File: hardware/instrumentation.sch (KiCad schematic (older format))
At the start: 5 parts

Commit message: Added TMUX1309 symbol
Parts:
- added U?: TMUX1309, Package_DFN_QFN:WQFN-16-1EP_3x3mm_P0.5mm_EP1.6x1.6mm, symbol mallard:TMUX1309
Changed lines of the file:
@@
+	1    0    0    -1
+$EndComp
+$Comp
+L mallard:TMUX1309 U?
+U 1 1 610A2355
+P 6250 750
+F 0 "U?" H 6250 875 50  0000 C CNN
+F 1 "TMUX1309" H 6250 784 50  0000 C CNN
+F 2 "Package_DFN_QFN:WQFN-16-1EP_3x3mm_P0.5mm_EP1.6x1.6mm" H 6250 -1150 50  0001 C CNN
+F 3 "https://www.ti.com/lit/ds/symlink/tmux1309.pdf" H 6250 750 50  0001 C CNN
+	1    6250 750
 	1    0    0    -1
 $EndComp

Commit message: Added Instrumentation Circuits
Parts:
- removed U?: SN74HCS153, symbol mallard:SN74HCS153
- added 10k (x4), 1k, 20k (x2), 30k, 9k: R, symbol Device:R
- added Eh1, Eh2, Eh3: Eh Electrode, symbol Connector_Generic:Conn_01x01
- added MUX2: TMUX1309, Package_DFN_QFN:WQFN-16-1EP_3x3mm_P0.5mm_EP1.6x1.6mm, symbol mallard:TMUX1309
- added Ref1: Ref Electrode, symbol Connector_Generic:Conn_01x01
- added SM1, SM2, SM3: Oct Soil Moisture, symbol Connector_Generic:Conn_01x03
- gave numbers to parts that had none: 5
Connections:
- net labels added: +1V0, +3V3, -3V3, GND, VDD
- wire segments 0 -> 68
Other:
- note added: "Eh Sensor Output"
- note added: "Reference Electrode Output"
- note added: "Soil Moisture Output"
- note added: "Temperature Sensor Output"
- moved on the sheet: MUX1, OP1, Temp1, Temp2, Temp3

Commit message: Added all Digikey part numbers. Started MC schematic. Fixed the reference number on some symbols.
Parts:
- removed 10k (x4), 1k, 20k (x2), 30k, 9k: R, symbol Device:R
- removed MUX1, MUX2: TMUX1309, Package_DFN_QFN:WQFN-16-1EP_3x3mm_P0.5mm_EP1.6x1.6mm, symbol mallard:TMUX1309
- removed OP1: LMV554, symbol mallard:LMV554
- removed Temp1, Temp2, Temp3: TMP235, symbol mallard:TMP235
- added R10: 9.1k, symbol Device:R
- added R11, R8: 20k, symbol Device:R
- added R3, R4, R5, R9: 10k, symbol Device:R
- added R6: 1k, symbol Device:R
- added R7: 30k, symbol Device:R
- added U2, U3: TMUX1309, Package_DFN_QFN:WQFN-16-1EP_3x3mm_P0.5mm_EP1.6x1.6mm, symbol mallard:TMUX1309
- added U4: LMV554, symbol mallard:LMV554
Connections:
- net labels added: Eh_Sense, Moisture_Sense, Ref_Out, Temp_Sense
- net labels removed: VDD
- wire segments 68 -> 61
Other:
- note added: "Needed New Temp sensors\n"
- note removed: "Eh Sensor Output"
- note removed: "Reference Electrode Output"
- note removed: "Temperature Sensor Output"

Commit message: Finished MC design
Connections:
- net MUX1_A1: now reaches U2.10 (A0)
- net MUX1_EN: now reaches U2.6 (EN)
- net MUX1_A0: now reaches U2.9 (A1)
- net MUX2_A1: now reaches U3.10 (A0)
- net MUX2_EN: now reaches U3.6 (EN)
- net MUX2_A0: now reaches U3.9 (A1)
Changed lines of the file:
@@
 	2800 2550 4150 2550
 Wire Wire Line
-	3550 1900 3550 2450
-Wire Wire Line
-	3800 1250 3800 2350
+	3100 1900 3100 2450
+Wire Wire Line
+	3300 1250 3300 2350
 Wire Wire Line
 	2800 3350 3250 3350
@@
 	3750 3050 4150 3050
 Wire Wire Line
-	3800 2350 4150 2350
-Wire Wire Line
-	2800 1250 3800 1250
-Wire Wire Line
-	3550 2450 4150 2450
-Wire Wire Line
-	2800 1900 3550 1900
+	3300 2350 4150 2350
+Wire Wire Line
+	2800 1250 3300 1250
+Wire Wire Line
+	3100 2450 4150 2450
+Wire Wire Line
+	2800 1900 3100 1900
 Wire Wire Line
 	5100 2850 4950 2850
@@
 Text Notes 2850 4800 0    50   ~ 0
 Needed New Temp sensors\n
+Text GLabel 4050 1850 0    50   Input ~ 0
+MUX1_EN
+Text GLabel 4050 2050 0    50   Input ~ 0
+MUX1_A0
+Text GLabel 4050 2150 0    50   Input ~ 0
+MUX1_A1
+Wire Wire Line
+	4150 1850 4050 1850
+Wire Wire Line
+	4150 2050 4050 2050
+Wire Wire Line
+	4150 2150 4050 2150
+Text GLabel 4100 4250 0    50   Input ~ 0
+MUX2_EN
+Wire Wire Line
+	4100 4250 4200 4250
+Text GLabel 4100 4450 0    50   Input ~ 0
+MUX2_A0
+Text GLabel 4100 4550 0    50   Input ~ 0
+MUX2_A1
+Wire Wire Line
+	4200 4450 4100 4450
+Wire Wire Line
+	4200 4550 4100 4550
 $EndSCHEMATC

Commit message: Not sure what changes I made sry
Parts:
- U4: Digikey LMP7721MA/NOPB-ND‎ -> (none)
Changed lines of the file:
@@
 F 2 "" H 7500 1600 50  0001 C CNN
 F 3 "https://www.ti.com/lit/ds/symlink/lmv551.pdf?HQS=dis-dk-null-digikeymode-dsf-pf-null-wwe&ts=1626469395066&ref_url=https%253A%252F%252Fwww.ti.com%252Fgeneral%252Fdocs%252Fsuppproductinfo.tsp%253FdistId%253D10%2526gotoUrl%253Dhttps%253A%252F%252Fwww.ti.com%252Flit%252Fgpn%252Flmv551" H 7500 1600 50  0001 C CNN
-F 4 "LMP7721MA/NOPB-ND‎" H 7500 2500 50  0001 C CNN "Digikey"
+F 4 "" H 7500 2500 50  0001 C CNN "Digikey"
 	1    7500 2500
 	1    0    0    -1

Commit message: House Keeping Tasks
 - Modified parts list parameters for various parts
 - Assigned Ref Des to components
 - Changed TPS717 symbol and feedback resistors
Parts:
- R10, R11, R4, R6, R7, R8: footprint (none) -> Resistor_SMD:R_0201_0603Metric_Pad0.64x0.40mm_HandSolder
- R3, R5, R9: footprint (none) -> Resistor_SMD:R_0201_0603Metric_Pad0.64x0.40mm_HandSolder; Manufacturer ‎RC0603DR-0710KL‎ -> (none)
- U4: footprint (none) -> Package_SO:TSSOP-14_4.4x5mm_P0.65mm; Digikey (none) -> 296-51370-1-ND
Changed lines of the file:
@@
 F 0 "R3" V 5043 2850 50  0000 C CNN
 F 1 "10k" V 5134 2850 50  0000 C CNN
-F 2 "" V 5180 2850 50  0001 C CNN
-F 3 "~" H 5250 2850 50  0001 C CNN
+F 2 "Resistor_SMD:R_0201_0603Metric_Pad0.64x0.40mm_HandSolder" V 5180 2850 50  0001 C CNN
+F 3 "https://www.yageo.com/upload/media/product/productsearch/datasheet/rchip/PYu-RC_Group_51_RoHS_L_11.pdf" H 5250 2850 50  0001 C CNN
 F 4 "13-RC0603DR-0710KLCT-ND‎" V 5250 2850 50  0001 C CNN "Digikey"
-F 5 "‎RC0603DR-0710KL‎" V 5250 2850 50  0001 C CNN "Manufacturer"
 	1    5250 2850
 	0    1    1    0
@@
 F 0 "R8" V 7243 1750 50  0000 C CNN
 F 1 "20k" V 7334 1750 50  0000 C CNN
-F 2 "" V 7380 1750 50  0001 C CNN
-F 3 "~" H 7450 1750 50  0001 C CNN
+F 2 "Resistor_SMD:R_0201_0603Metric_Pad0.64x0.40mm_HandSolder" V 7380 1750 50  0001 C CNN
+F 3 "https://industrial.panasonic.com/cdbs/www-data/pdf/RDM0000/AOA0000C328.pdf" H 7450 1750 50  0001 C CNN
 F 4 "‎P20429CT-ND‎" V 7450 1750 50  0001 C CNN "Digikey"
 	1    7450 1750
@@
 F 0 "R7" V 7243 1350 50  0000 C CNN
 F 1 "30k" V 7334 1350 50  0000 C CNN
-F 2 "" V 7380 1350 50  0001 C CNN
-F 3 "~" H 7450 1350 50  0001 C CNN
+F 2 "Resistor_SMD:R_0201_0603Metric_Pad0.64x0.40mm_HandSolder" V 7380 1350 50  0001 C CNN
+F 3 "https://www.yageo.com/upload/media/product/productsearch/datasheet/rchip/PYu-RT_1-to-0.01_RoHS_L_12.pdf" H 7450 1350 50  0001 C CNN
 F 4 "311-30KDCT-ND‎" V 7450 1350 50  0001 C CNN "Digikey"
 	1    7450 1350
@@
 F 0 "U4" H 7500 2675 50  0000 C CNN
 F 1 "LMV554" H 7500 2584 50  0000 C CNN
-F 2 "" H 7500 1600 50  0001 C CNN
+F 2 "Package_SO:TSSOP-14_4.4x5mm_P0.65mm" H 7500 1600 50  0001 C CNN
 F 3 "https://www.ti.com/lit/ds/symlink/lmv551.pdf?HQS=dis-dk-null-digikeymode-dsf-pf-null-wwe&ts=1626469395066&ref_url=https%253A%252F%252Fwww.ti.com%252Fgeneral%252Fdocs%252Fsuppproductinfo.tsp%253FdistId%253D10%2526gotoUrl%253Dhttps%253A%252F%252Fwww.ti.com%252Flit%252Fgpn%252Flmv551" H 7500 1600 50  0001 C CNN
-F 4 "" H 7500 2500 50  0001 C CNN "Digikey"
+F 4 "296-51370-1-ND" H 7500 2500 50  0001 C CNN "Digikey"
 	1    7500 2500
 	1    0    0    -1
@@
 F 0 "R6" H 7120 5146 50  0000 L CNN
 F 1 "1k" H 7120 5055 50  0000 L CNN
-F 2 "" V 6980 5100 50  0001 C CNN
-F 3 "~" H 7050 5100 50  0001 C CNN
+F 2 "Resistor_SMD:R_0201_0603Metric_Pad0.64x0.40mm_HandSolder" V 6980 5100 50  0001 C CNN
+F 3 "https://www.vishay.com/docs/20065/rcse3.pdf" H 7050 5100 50  0001 C CNN
 F 4 "541-2788-1-ND" H 7050 5100 50  0001 C CNN "Digikey"
 	1    7050 5100
@@
 F 0 "R10" V 7293 4850 50  0000 C CNN
 F 1 "9.1k" V 7384 4850 50  0000 C CNN
-F 2 "" V 7430 4850 50  0001 C CNN
-F 3 "~" H 7500 4850 50  0001 C CNN
+F 2 "Resistor_SMD:R_0201_0603Metric_Pad0.64x0.40mm_HandSolder" V 7430 4850 50  0001 C CNN
+F 3 "https://www.yageo.com/upload/media/product/productsearch/datasheet/rchip/PYu-RT_1-to-0.01_RoHS_L_12.pdf" H 7500 4850 50  0001 C CNN
 F 4 "YAG1756CT-ND‎" H 7500 4850 50  0001 C CNN "Digikey"
 	1    7500 4850
@@
 F 0 "R4" H 5830 2554 50  0000 R CNN
 F 1 "10k" H 5830 2645 50  0000 R CNN
-F 2 "" V 5830 2600 50  0001 C CNN
-F 3 "~" H 5900 2600 50  0001 C CNN
+F 2 "Resistor_SMD:R_0201_0603Metric_Pad0.64x0.40mm_HandSolder" V 5830 2600 50  0001 C CNN
+F 3 "https://www.yageo.com/upload/media/product/productsearch/datasheet/rchip/PYu-RC_Group_51_RoHS_L_11.pdf" H 5900 2600 50  0001 C CNN
 F 4 "13-RC0603DR-0710KLCT-ND‎" V 5900 2600 50  0001 C CNN "Digikey"
 	1    5900 2600
@@
 F 0 "R9" V 7243 2150 50  0000 C CNN
 F 1 "10k" V 7334 2150 50  0000 C CNN
-F 2 "" V 7380 2150 50  0001 C CNN
-F 3 "~" H 7450 2150 50  0001 C CNN
+F 2 "Resistor_SMD:R_0201_0603Metric_Pad0.64x0.40mm_HandSolder" V 7380 2150 50  0001 C CNN
+F 3 "https://www.yageo.com/upload/media/product/productsearch/datasheet/rchip/PYu-RC_Group_51_RoHS_L_11.pdf" H 7450 2150 50  0001 C CNN
 F 4 "13-RC0603DR-0710KLCT-ND‎" V 7450 2150 50  0001 C CNN "Digikey"
-F 5 "‎RC0603DR-0710KL‎" V 7450 2150 50  0001 C CNN "Manufacturer"
 	1    7450 2150
 	0    1    1    0
@@
 F 0 "R5" H 6730 5854 50  0000 R CNN
 F 1 "10k" H 6730 5945 50  0000 R CNN
-F 2 "" V 6730 5900 50  0001 C CNN
-F 3 "~" H 6800 5900 50  0001 C CNN
+F 2 "Resistor_SMD:R_0201_0603Metric_Pad0.64x0.40mm_HandSolder" V 6730 5900 50  0001 C CNN
+F 3 "https://www.yageo.com/upload/media/product/productsearch/datasheet/rchip/PYu-RC_Group_51_RoHS_L_11.pdf" H 6800 5900 50  0001 C CNN
 F 4 "13-RC0603DR-0710KLCT-ND‎" V 6800 5900 50  0001 C CNN "Digikey"
-F 5 "‎RC0603DR-0710KL‎" V 6800 5900 50  0001 C CNN "Manufacturer"
 	1    6800 5900
 	-1   0    0    1
@@
 F 0 "R11" V 7293 5600 50  0000 C CNN
 F 1 "20k" V 7384 5600 50  0000 C CNN
-F 2 "" V 7430 5600 50  0001 C CNN
-F 3 "~" H 7500 5600 50  0001 C CNN
+F 2 "Resistor_SMD:R_0201_0603Metric_Pad0.64x0.40mm_HandSolder" V 7430 5600 50  0001 C CNN
+F 3 "https://industrial.panasonic.com/cdbs/www-data/pdf/RDM0000/AOA0000C328.pdf" H 7500 5600 50  0001 C CNN
 F 4 "‎P20429CT-ND‎" V 7500 5600 50  0001 C CNN "Digikey"
 	1    7500 5600

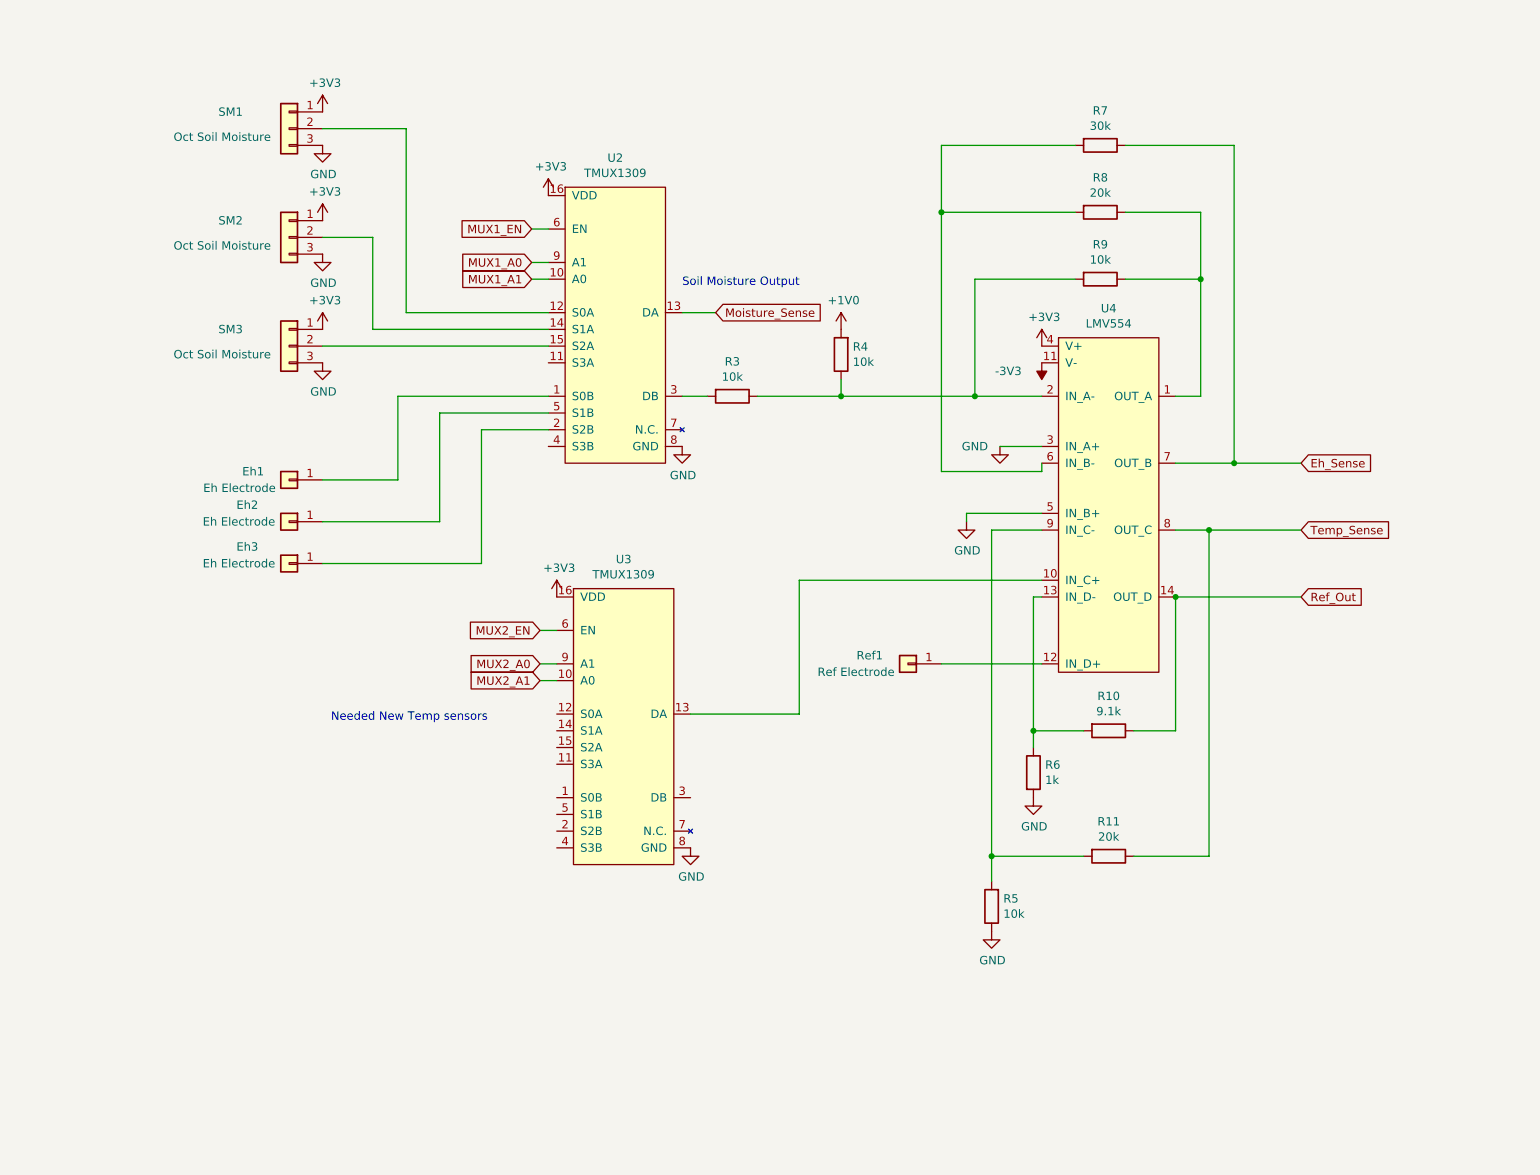
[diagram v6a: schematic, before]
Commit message: Added more ref des
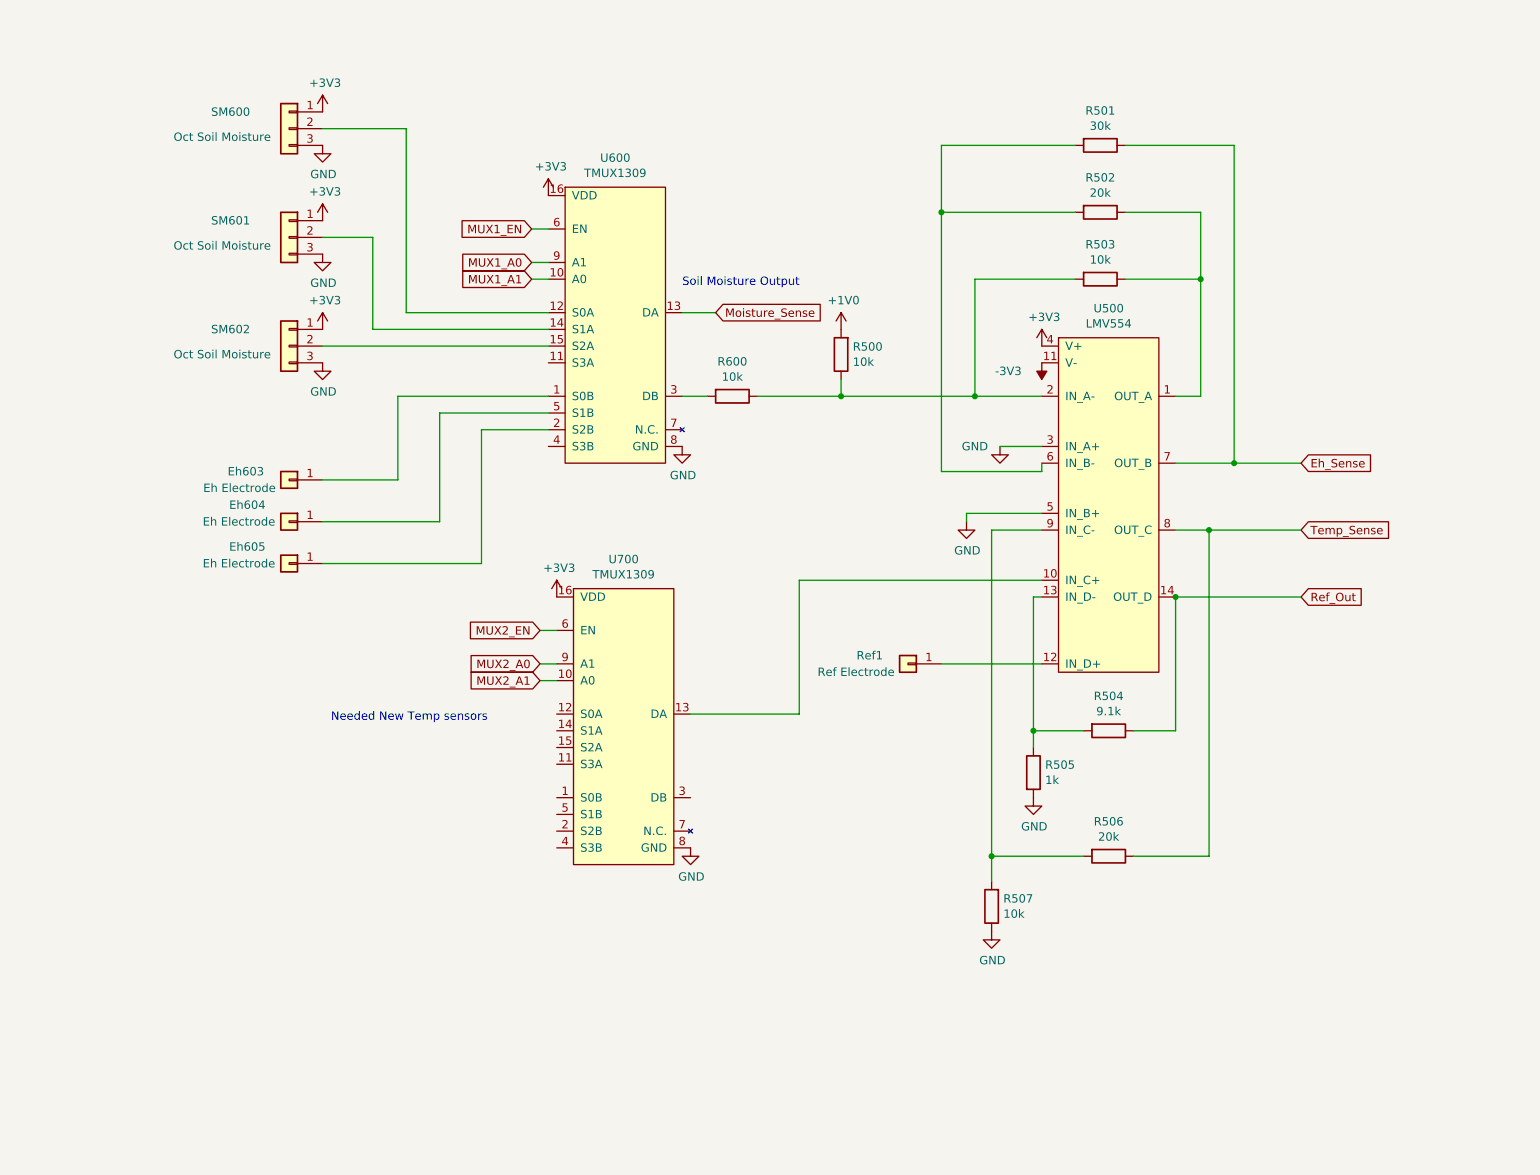
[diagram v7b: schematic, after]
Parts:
- renumbered Eh1 to Eh603, Eh2 to Eh604, Eh3 to Eh605, R4 to R500, R7 to R501, R8 to R502, R9 to R503, R10 to R504, R6 to R505, R11 to R506, R5 to R507, R3 to R600, SM1 to SM600, SM2 to SM601, SM3 to SM602, U4 to U500, U2 to U600, U3 to U700
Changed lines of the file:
@@
 $EndComp
 $Comp
-L Connector_Generic:Conn_01x01 Eh1
+L Connector_Generic:Conn_01x01 Eh603
 U 1 1 610DC20D
 P 2600 3350
-F 0 "Eh1" H 2750 3400 50  0000 L CNN
+F 0 "Eh603" H 2750 3400 50  0000 L CNN
 F 1 "Eh Electrode" H 2680 3301 50  0000 L CNN
 F 2 "" H 2600 3350 50  0001 C CNN
@@
 $EndComp
 $Comp
-L Connector_Generic:Conn_01x01 Eh2
+L Connector_Generic:Conn_01x01 Eh604
 U 1 1 610DD4BF
 P 2600 3600
-F 0 "Eh2" H 2850 3700 50  0000 C CNN
+F 0 "Eh604" H 2850 3700 50  0000 C CNN
 F 1 "Eh Electrode" H 2900 3600 50  0000 C CNN
 F 2 "" H 2600 3600 50  0001 C CNN
@@
 $EndComp
 $Comp
-L Connector_Generic:Conn_01x01 Eh3
+L Connector_Generic:Conn_01x01 Eh605
 U 1 1 610DDA62
 P 2600 3850
-F 0 "Eh3" H 2850 3950 50  0000 C CNN
+F 0 "Eh605" H 2850 3950 50  0000 C CNN
 F 1 "Eh Electrode" H 2900 3850 50  0000 C CNN
 F 2 "" H 2600 3850 50  0001 C CNN
@@
 $EndComp
 $Comp
-L Connector_Generic:Conn_01x03 SM1
+L Connector_Generic:Conn_01x03 SM600
 U 1 1 610E87B7
 P 2600 1250
-F 0 "SM1" H 2950 1350 50  0000 C CNN
+F 0 "SM600" H 2950 1350 50  0000 C CNN
 F 1 "Oct Soil Moisture " H 3000 1200 50  0000 C CNN
 F 2 "" H 2600 1250 50  0001 C CNN
@@
 $EndComp
 $Comp
-L Connector_Generic:Conn_01x03 SM2
+L Connector_Generic:Conn_01x03 SM601
 U 1 1 610F5909
 P 2600 1900
-F 0 "SM2" H 2950 2000 50  0000 C CNN
+F 0 "SM601" H 2950 2000 50  0000 C CNN
 F 1 "Oct Soil Moisture " H 3000 1850 50  0000 C CNN
 F 2 "" H 2600 1900 50  0001 C CNN
@@
 $EndComp
 $Comp
-L Connector_Generic:Conn_01x03 SM3
+L Connector_Generic:Conn_01x03 SM602
 U 1 1 610F6592
 P 2600 2550
-F 0 "SM3" H 2950 2650 50  0000 C CNN
+F 0 "SM602" H 2950 2650 50  0000 C CNN
 F 1 "Oct Soil Moisture " H 3000 2500 50  0000 C CNN
 F 2 "" H 2600 2550 50  0001 C CNN
@@
 	6850 3150 7100 3150
 $Comp
-L mallard:TMUX1309 U2
+L mallard:TMUX1309 U600
 U 1 1 61595D93
 P 4550 1550
-F 0 "U2" H 4550 1675 50  0000 C CNN
+F 0 "U600" H 4550 1675 50  0000 C CNN
 F 1 "TMUX1309" H 4550 1584 50  0000 C CNN
 F 2 "Package_DFN_QFN:WQFN-16-1EP_3x3mm_P0.5mm_EP1.6x1.6mm" H 4550 -350 50  0001 C CNN
@@
 $EndComp
 $Comp
-L Device:R R3
+L Device:R R600
 U 1 1 6159B70F
 P 5250 2850
-F 0 "R3" V 5043 2850 50  0000 C CNN
+F 0 "R600" V 5043 2850 50  0000 C CNN
 F 1 "10k" V 5134 2850 50  0000 C CNN
 F 2 "Resistor_SMD:R_0201_0603Metric_Pad0.64x0.40mm_HandSolder" V 5180 2850 50  0001 C CNN
@@
 $EndComp
 $Comp
-L Device:R R8
+L Device:R R502
 U 1 1 6159EF44
 P 7450 1750
-F 0 "R8" V 7243 1750 50  0000 C CNN
+F 0 "R502" V 7243 1750 50  0000 C CNN
 F 1 "20k" V 7334 1750 50  0000 C CNN
 F 2 "Resistor_SMD:R_0201_0603Metric_Pad0.64x0.40mm_HandSolder" V 7380 1750 50  0001 C CNN
@@
 $EndComp
 $Comp
-L Device:R R7
+L Device:R R501
 U 1 1 615A0EFD
 P 7450 1350
-F 0 "R7" V 7243 1350 50  0000 C CNN
+F 0 "R501" V 7243 1350 50  0000 C CNN
 F 1 "30k" V 7334 1350 50  0000 C CNN
 F 2 "Resistor_SMD:R_0201_0603Metric_Pad0.64x0.40mm_HandSolder" V 7380 1350 50  0001 C CNN
@@
 $EndComp
 $Comp
-L mallard:LMV554 U4
+L mallard:LMV554 U500
 U 1 1 615A28E5
 P 7500 2500
-F 0 "U4" H 7500 2675 50  0000 C CNN
+F 0 "U500" H 7500 2675 50  0000 C CNN
 F 1 "LMV554" H 7500 2584 50  0000 C CNN
 F 2 "Package_SO:TSSOP-14_4.4x5mm_P0.65mm" H 7500 1600 50  0001 C CNN
@@
 Connection ~ 7900 4050
 $Comp
-L Device:R R6
+L Device:R R505
 U 1 1 615A675D
 P 7050 5100
-F 0 "R6" H 7120 5146 50  0000 L CNN
+F 0 "R505" H 7120 5146 50  0000 L CNN
 F 1 "1k" H 7120 5055 50  0000 L CNN
 F 2 "Resistor_SMD:R_0201_0603Metric_Pad0.64x0.40mm_HandSolder" V 6980 5100 50  0001 C CNN
@@
 $EndComp
 $Comp
-L Device:R R10
+L Device:R R504
 U 1 1 615A70C7
 P 7500 4850
-F 0 "R10" V 7293 4850 50  0000 C CNN
+F 0 "R504" V 7293 4850 50  0000 C CNN
 F 1 "9.1k" V 7384 4850 50  0000 C CNN
 F 2 "Resistor_SMD:R_0201_0603Metric_Pad0.64x0.40mm_HandSolder" V 7430 4850 50  0001 C CNN
@@
 $EndComp
 $Comp
-L Device:R R4
+L Device:R R500
 U 1 1 615A7B6B
 P 5900 2600
-F 0 "R4" H 5830 2554 50  0000 R CNN
+F 0 "R500" H 5830 2554 50  0000 R CNN
 F 1 "10k" H 5830 2645 50  0000 R CNN
 F 2 "Resistor_SMD:R_0201_0603Metric_Pad0.64x0.40mm_HandSolder" V 5830 2600 50  0001 C CNN
@@
 $EndComp
 $Comp
-L Device:R R9
+L Device:R R503
 U 1 1 615A829C
 P 7450 2150
-F 0 "R9" V 7243 2150 50  0000 C CNN
+F 0 "R503" V 7243 2150 50  0000 C CNN
 F 1 "10k" V 7334 2150 50  0000 C CNN
 F 2 "Resistor_SMD:R_0201_0603Metric_Pad0.64x0.40mm_HandSolder" V 7380 2150 50  0001 C CNN
@@
 $EndComp
 $Comp
-L Device:R R5
+L Device:R R507
 U 1 1 615A8D1F
 P 6800 5900
-F 0 "R5" H 6730 5854 50  0000 R CNN
+F 0 "R507" H 6730 5854 50  0000 R CNN
 F 1 "10k" H 6730 5945 50  0000 R CNN
 F 2 "Resistor_SMD:R_0201_0603Metric_Pad0.64x0.40mm_HandSolder" V 6730 5900 50  0001 C CNN
@@
 $EndComp
 $Comp
-L Device:R R11
+L Device:R R506
 U 1 1 615AA078
 P 7500 5600
-F 0 "R11" V 7293 5600 50  0000 C CNN
+F 0 "R506" V 7293 5600 50  0000 C CNN
 F 1 "20k" V 7384 5600 50  0000 C CNN
 F 2 "Resistor_SMD:R_0201_0603Metric_Pad0.64x0.40mm_HandSolder" V 7430 5600 50  0001 C CNN
@@
 Ref_Out
 $Comp
-L mallard:TMUX1309 U3
+L mallard:TMUX1309 U700
 U 1 1 615A1290
 P 4600 3950
-F 0 "U3" H 4600 4075 50  0000 C CNN
+F 0 "U700" H 4600 4075 50  0000 C CNN
 F 1 "TMUX1309" H 4600 3984 50  0000 C CNN
 F 2 "Package_DFN_QFN:WQFN-16-1EP_3x3mm_P0.5mm_EP1.6x1.6mm" H 4600 2050 50  0001 C CNN
